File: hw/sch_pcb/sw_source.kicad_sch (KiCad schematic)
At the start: 37 parts, among them U1 TPS631000DRLR

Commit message: Update and correct values from manufacturing process.
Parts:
- R4: UST_ID (none) -> 5c70984612875079b91f899f
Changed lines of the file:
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@@
       (effects (font (size 1 1)) hide)
     )
-    (property "UST_ID" "" (at 77.47 149.86 0)
+    (property "UST_ID" "5c70984612875079b91f899f" (at 77.47 149.86 0)
       (effects (font (size 1 1)) hide)
     )
@@
       (effects (font (size 1 1)) hide)
     )
-    (property "UST_ID" "" (at 83.82 97.79 0)
-      (effects (font (size 1 1)) hide)
-    )
+    (property "UST_ID" "5c70984612875079b91f899f" (at 83.82 97.79 0)
+      (effects (font (size 1 1)) hide)
+    )

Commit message: Update the commponent values according to actual component values used during manufacturing.
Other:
- company: MLAB.cz -> MLAB.cz, roman-dvorak
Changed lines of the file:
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@@
   (title_block
     (title "BATDATUNTI01")
-    (rev "01A")
-    (company "MLAB.cz")
-    (comment 2 "Universial battery and data storage unit.")
+    (rev "B")
+    (company "MLAB.cz, roman-dvorak")
+    (comment 2 "Universal battery and data storage unit.")
   )
   (junction (at 156.21 91.44) (diameter 0) (color 0 0 0 0)

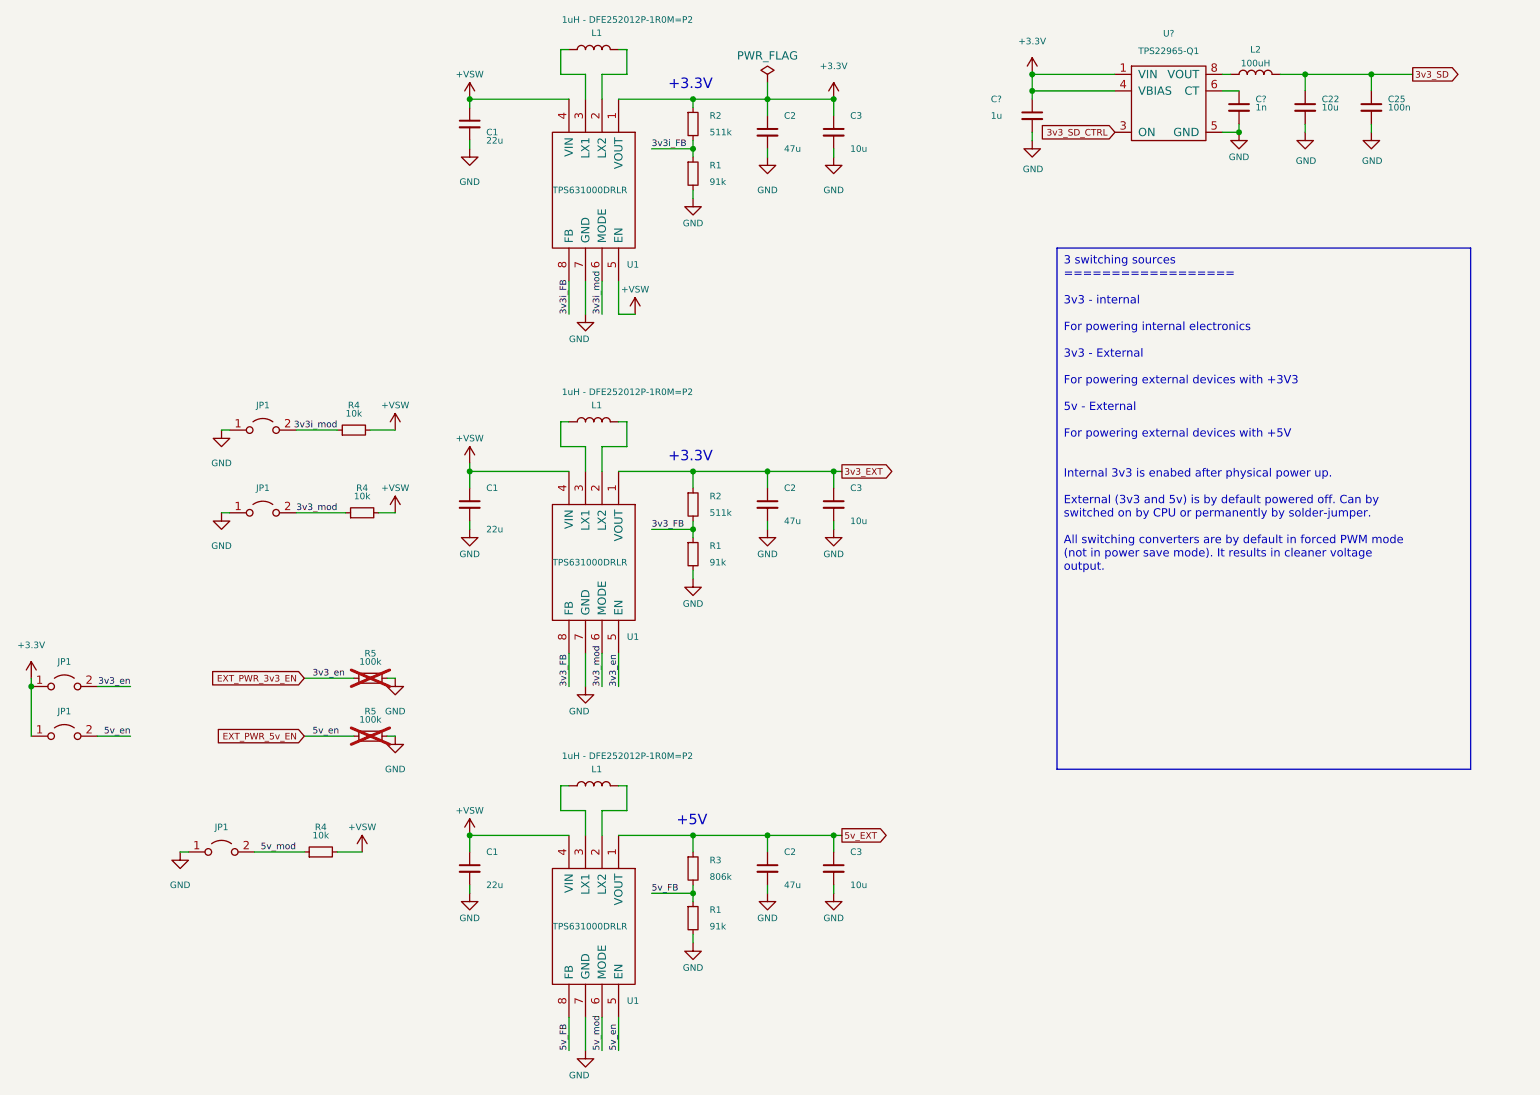
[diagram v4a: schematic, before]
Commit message: Convert to KiCAD 9 Add CR2032 battery holder to avoid RTC reset with removed accumulators.
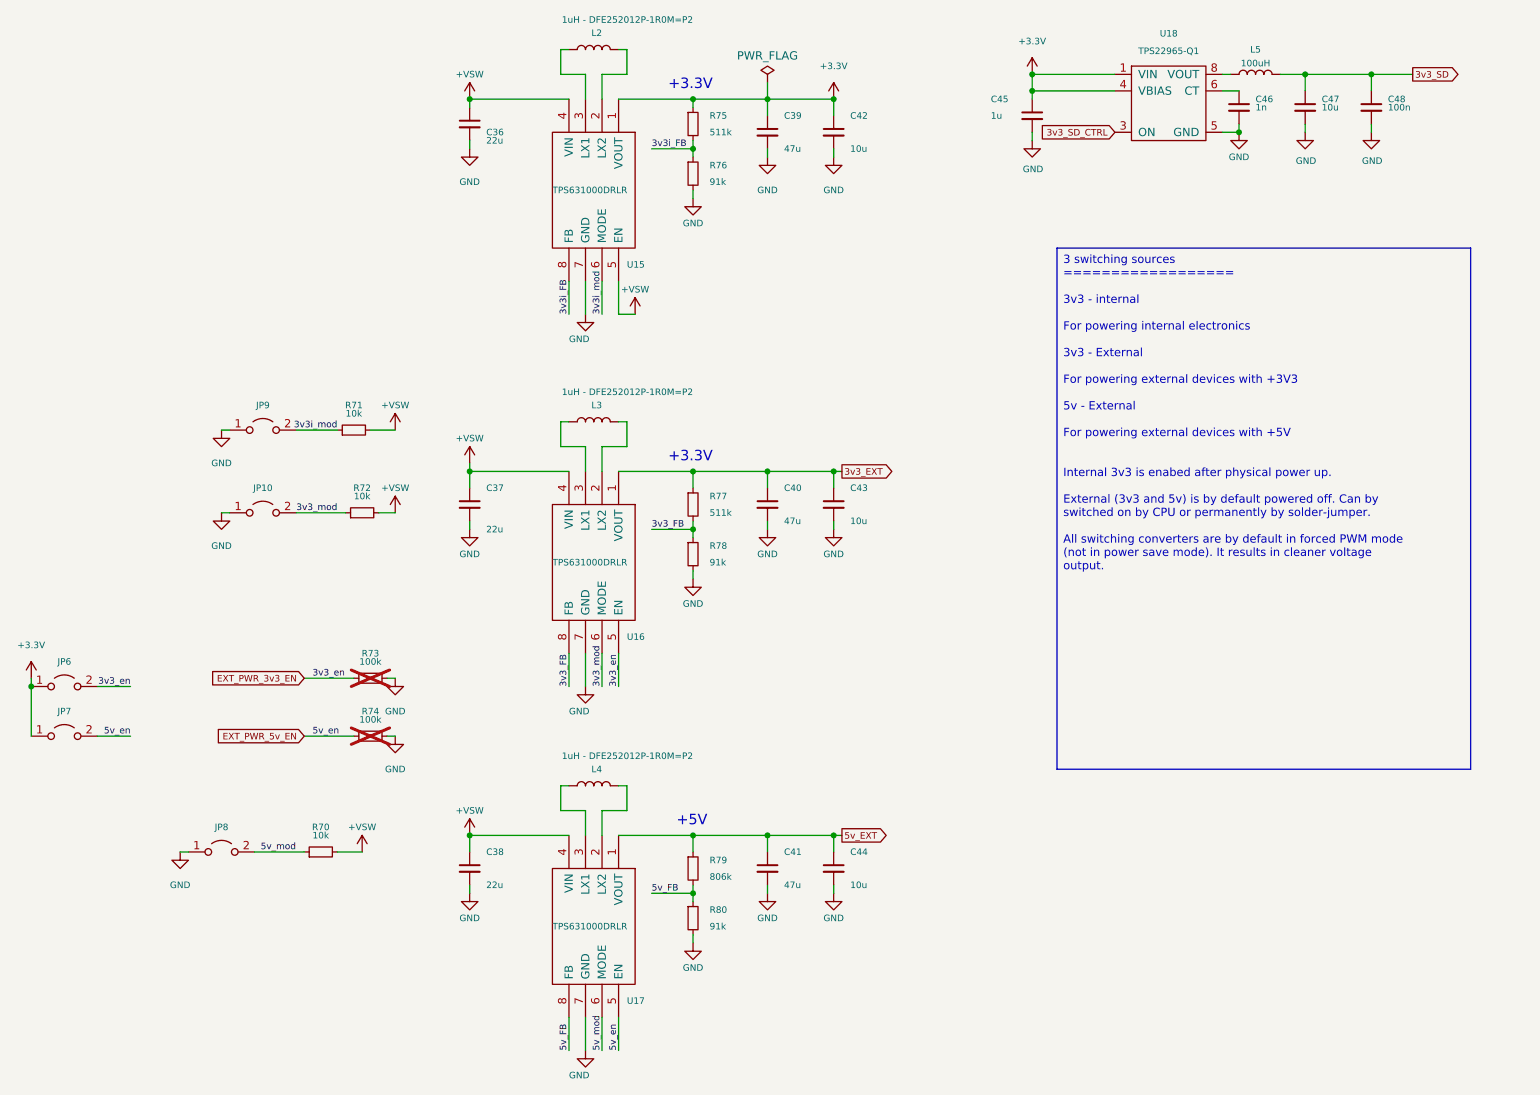
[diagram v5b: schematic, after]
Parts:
- gave numbers to parts that had none: 3
- renumbered C1 to C36, C1 to C37, C1 to C38, C2 to C39, C2 to C40, C2 to C41, C3 to C42, C3 to C43, C3 to C44, C22 to C47, C25 to C48, JP1 to JP10, JP1 to JP6, JP1 to JP7, JP1 to JP8, JP1 to JP9, L1 to L2, L1 to L3, L1 to L4, L2 to L5, R4 to R70, R4 to R71, R4 to R72, R5 to R73, R5 to R74, R2 to R75, R1 to R76, R2 to R77, R1 to R78, R3 to R79, R1 to R80, U1 to U15, U1 to U16, U1 to U17

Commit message: Update UST_IDs.
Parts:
- R71: UST_ID (none) -> 5c70984612875079b91f899f
- R73, R74: value 100k -> 91k; UST_ID (none) -> 5c70984712875079b91f8a95
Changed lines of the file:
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@@
 			)
 		)
-		(property "UST_ID" ""
+		(property "UST_ID" " 5c70984612875079b91f899f"
 			(at 82.55 85.09 0)
 			(effects
@@
 			)
 		)
-		(property "Value" "100k"
+		(property "Value" "91k"
 			(at 85.09 129.54 90)
 			(effects
@@
 			)
 		)
-		(property "UST_ID" ""
+		(property "UST_ID" "5c70984712875079b91f8a95"
 			(at 85.09 132.08 0)
 			(effects
@@
 			)
 		)
-		(property "Value" "100k"
+		(property "Value" "91k"
 			(at 85.09 120.65 90)
 			(effects
@@
 			)
 		)
-		(property "UST_ID" ""
+		(property "UST_ID" "5c70984712875079b91f8a95"
 			(at 85.09 123.19 0)
 			(effects

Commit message: Repair white characters in UST_ID fields.
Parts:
- R71: UST_ID 5c70984612875079b91f899f -> 5c70984612875079b91f899f
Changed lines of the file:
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@@
 			)
 		)
-		(property "UST_ID" " 5c70984612875079b91f899f"
+		(property "UST_ID" "5c70984612875079b91f899f"
 			(at 82.55 85.09 0)
 			(effects
